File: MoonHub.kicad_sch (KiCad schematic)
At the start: 36 parts, among them U1 SRV05-4, U2 SRV05-4, U3 CH334U, U4 TPS2552DBVR, U5 SRV05-4, U6 SRV05-4, U7 SRV05-4, Y1 12MHz

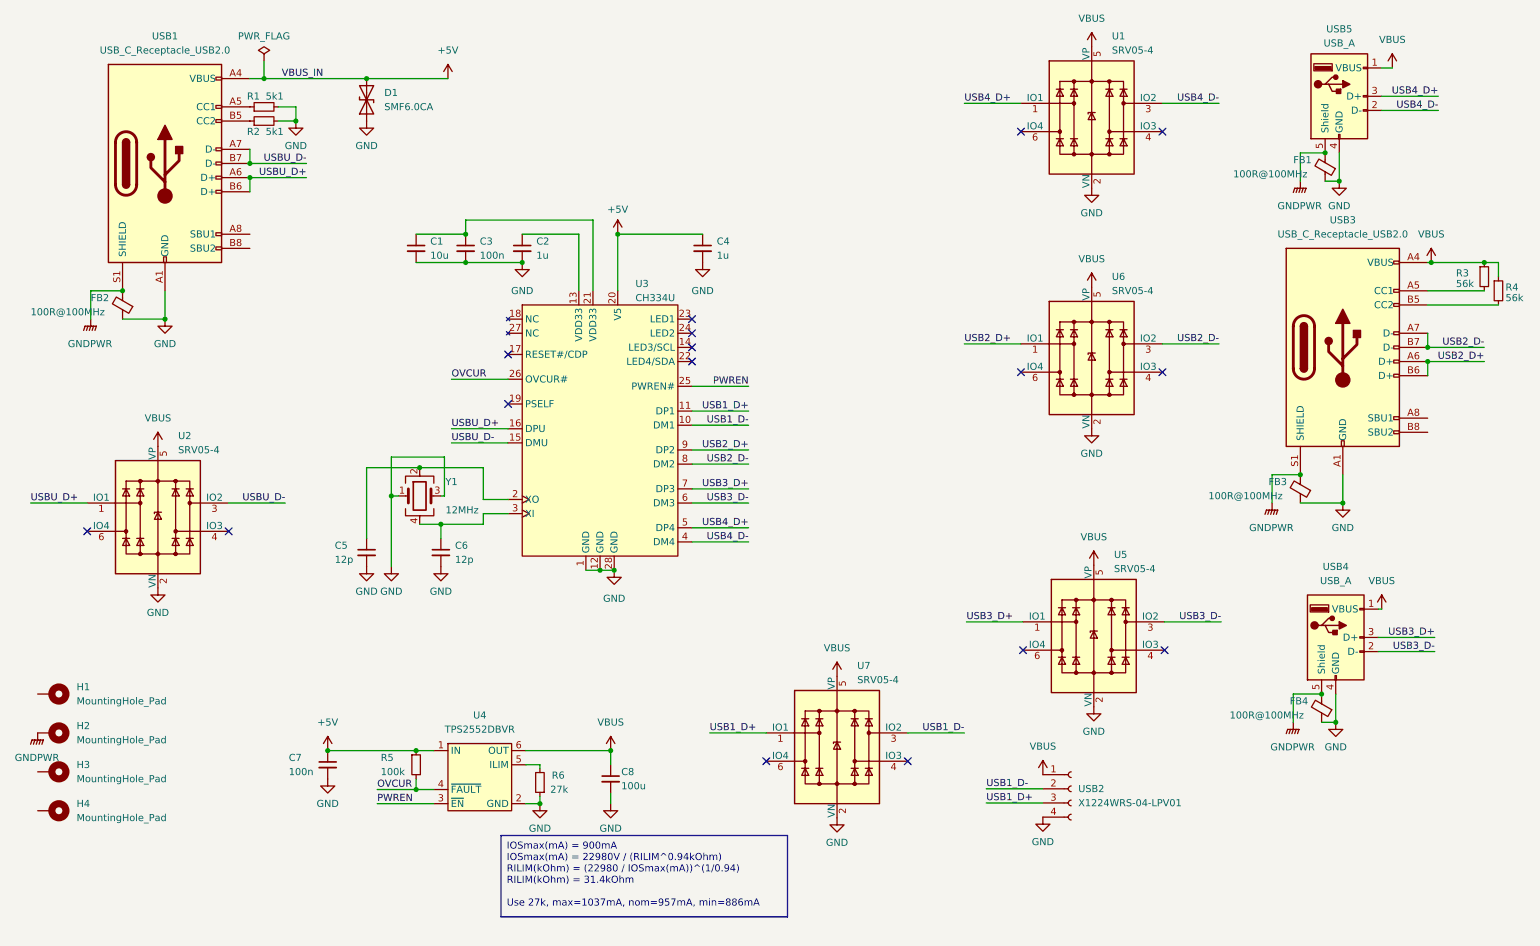
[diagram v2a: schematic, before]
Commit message: move uDB connector & switch current limit
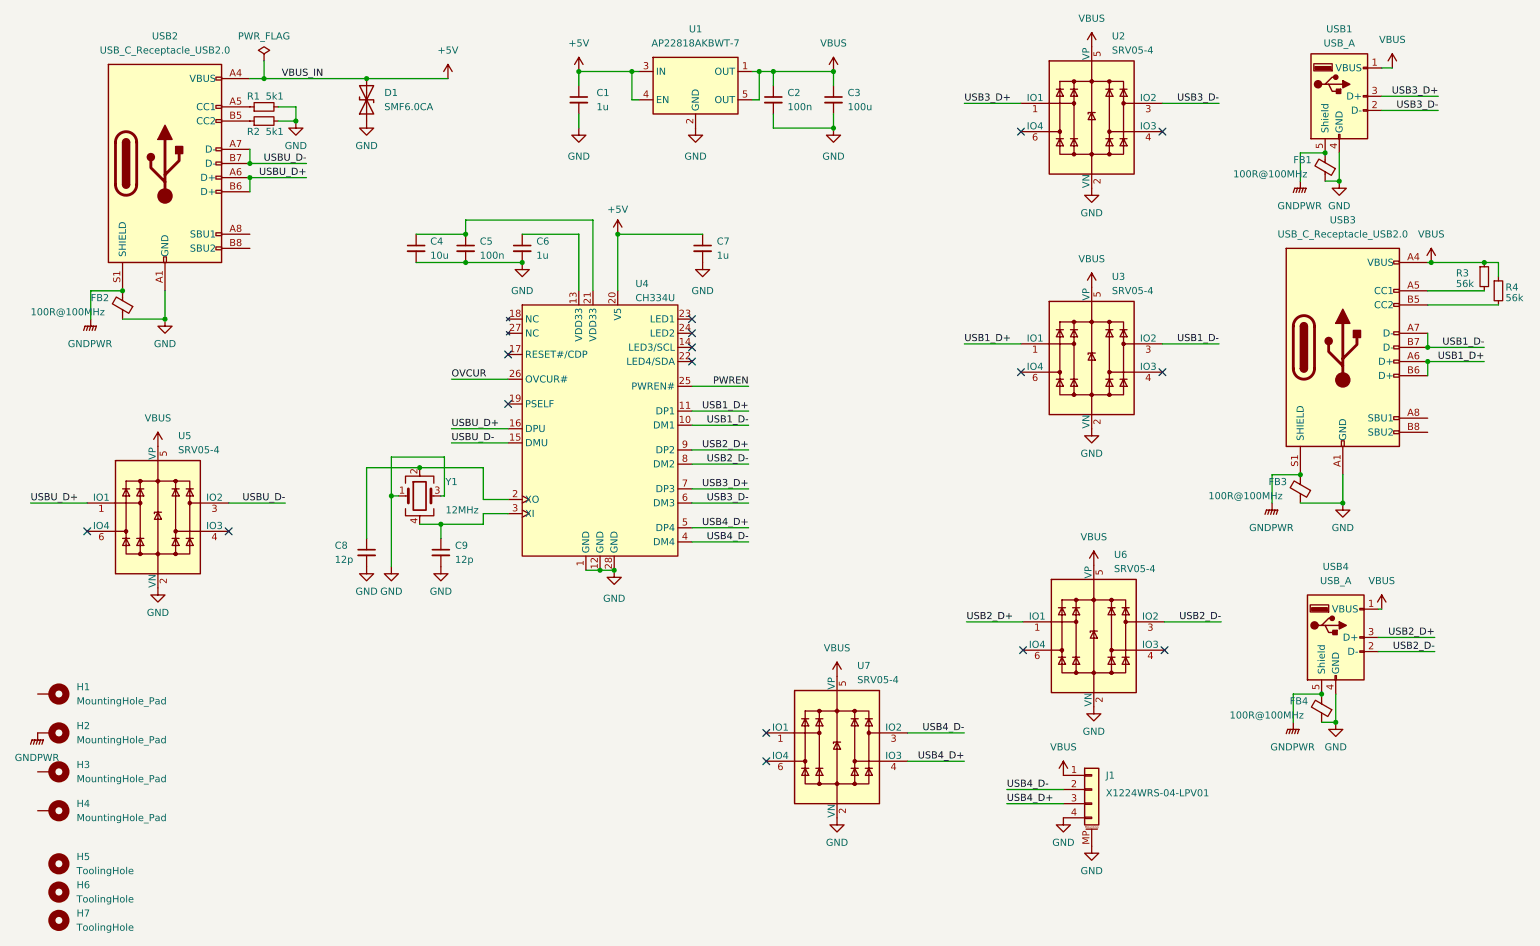
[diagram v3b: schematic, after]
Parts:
- removed C7: 100n, Capacitor_SMD:C_0805_2012Metric, symbol Device:C_Small
- removed C8: 100u, Capacitor_SMD:C_1206_3216Metric, symbol Device:C_Small
- removed R5: 100k, Resistor_SMD:R_0603_1608Metric, symbol Device:R_Small
- removed R6: 27k, Resistor_SMD:R_0603_1608Metric, symbol Device:R_Small
- removed U4: TPS2552DBVR, Package_TO_SOT_SMD:SOT-23-6, symbol MoonHub:TPS2552/53
- removed USB2: X1224WRS-04-LPV01, MoonHub:PicoEZMate-Reinforced-Lite, symbol Connector:Conn_01x04_Socket
- added C1: 1u, Capacitor_SMD:C_0402_1005Metric, symbol Device:C_Small
- added C2: 100n, Capacitor_SMD:C_0402_1005Metric, symbol Device:C_Small
- added C3: 100u, Capacitor_SMD:C_1206_3216Metric, symbol Device:C_Small
- added H5, H6, H7: ToolingHole, MoonHub:JLC-Tooling-Hole, symbol Mechanical:MountingHole
- added J1: X1224WRS-04-LPV01, MoonHub:UDB-PicoEZMate-Reinforced-Alt, symbol Connector_Generic_MountingPin:Conn_01x04_MountingPin
- added U1: AP22818AKBWT-7, Package_TO_SOT_SMD:SOT-23-5, symbol Power_Management:AP22814AW5
- C5: renamed from C3; footprint Capacitor_SMD:C_0805_2012Metric -> Capacitor_SMD:C_0402_1005Metric
- renumbered C1 to C4, C2 to C6, C4 to C7, C5 to C8, C6 to C9, U1 to U2, U6 to U3, U3 to U4, U2 to U5, U5 to U6, USB5 to USB1, USB1 to USB2
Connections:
- net +5V: now also C1.1, U1.3 (IN), U1.4 (EN)
- net GND: now also C1.2, C2.2, C3.2, J1.4 (Pin_4), J1.MP (MountPin), U1.2 (GND)
- net USB1_D+: now also U3.1 (IO1), USB3.A6 (D+), USB3.B6 (D+); no longer U7.1 (IO1)
- net USB1_D-: now also U3.3 (IO2), USB3.A7 (D-), USB3.B7 (D-); no longer U7.3 (IO2)
- net USB2_D+: now also U6.1 (IO1), USB4.3 (D+); no longer U3.1 (IO1), USB3.A6 (D+), USB3.B6 (D+)
- net USB2_D-: now also U6.3 (IO2), USB4.2 (D-); no longer U3.3 (IO2), USB3.A7 (D-), USB3.B7 (D-)
- net USB3_D+: now also U2.1 (IO1), USB1.3 (D+); no longer U6.1 (IO1), USB4.3 (D+)
- net USB3_D-: now also U2.3 (IO2), USB1.2 (D-); no longer U6.3 (IO2), USB4.2 (D-)
- net USB4_D+: now also U7.4 (IO3), J1.3 (Pin_3); no longer U2.1 (IO1), USB1.3 (D+)
- net USB4_D-: now also U7.3 (IO2), J1.2 (Pin_2); no longer U2.3 (IO2), USB1.2 (D-)
- net VBUS: now also C2.1, C3.1, J1.1 (Pin_1), U1.1 (OUT), U1.5 (OUT)

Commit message: redo esd protection
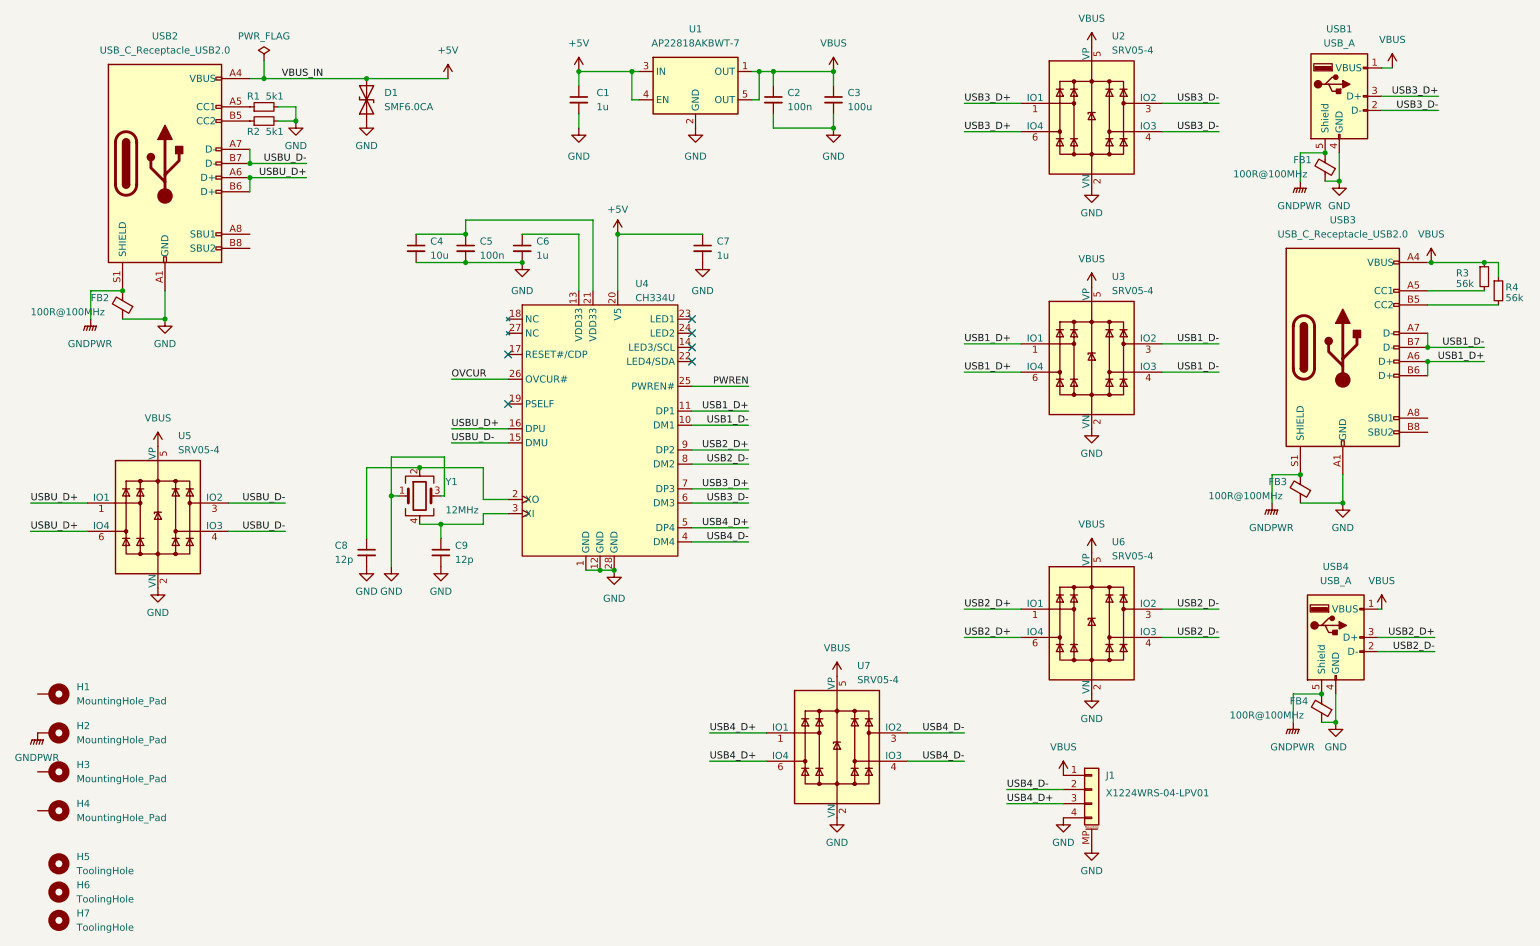
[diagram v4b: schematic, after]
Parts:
- U2, U3, U5, U6, U7: footprint PCM_marbastlib-various:SOT-23-6-routable -> Package_TO_SOT_SMD:SOT-23-6
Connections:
- net USB1_D+: now also U3.6 (IO4)
- net USB1_D-: now also U3.4 (IO3)
- net USB2_D+: now also U6.6 (IO4)
- net USB2_D-: now also U6.4 (IO3)
- net USB3_D+: now also U2.6 (IO4)
- net USB3_D-: now also U2.4 (IO3)
- net USB4_D+: now also U7.1 (IO1), U7.6 (IO4); no longer U7.4 (IO3)
- net USB4_D-: now also U7.4 (IO3)
- net USBU_D+: now also U5.6 (IO4)
- net USBU_D-: now also U5.4 (IO3)
- no-connect marks 16 -> 6
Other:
- moved on the sheet: U6

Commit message: change usb esd array
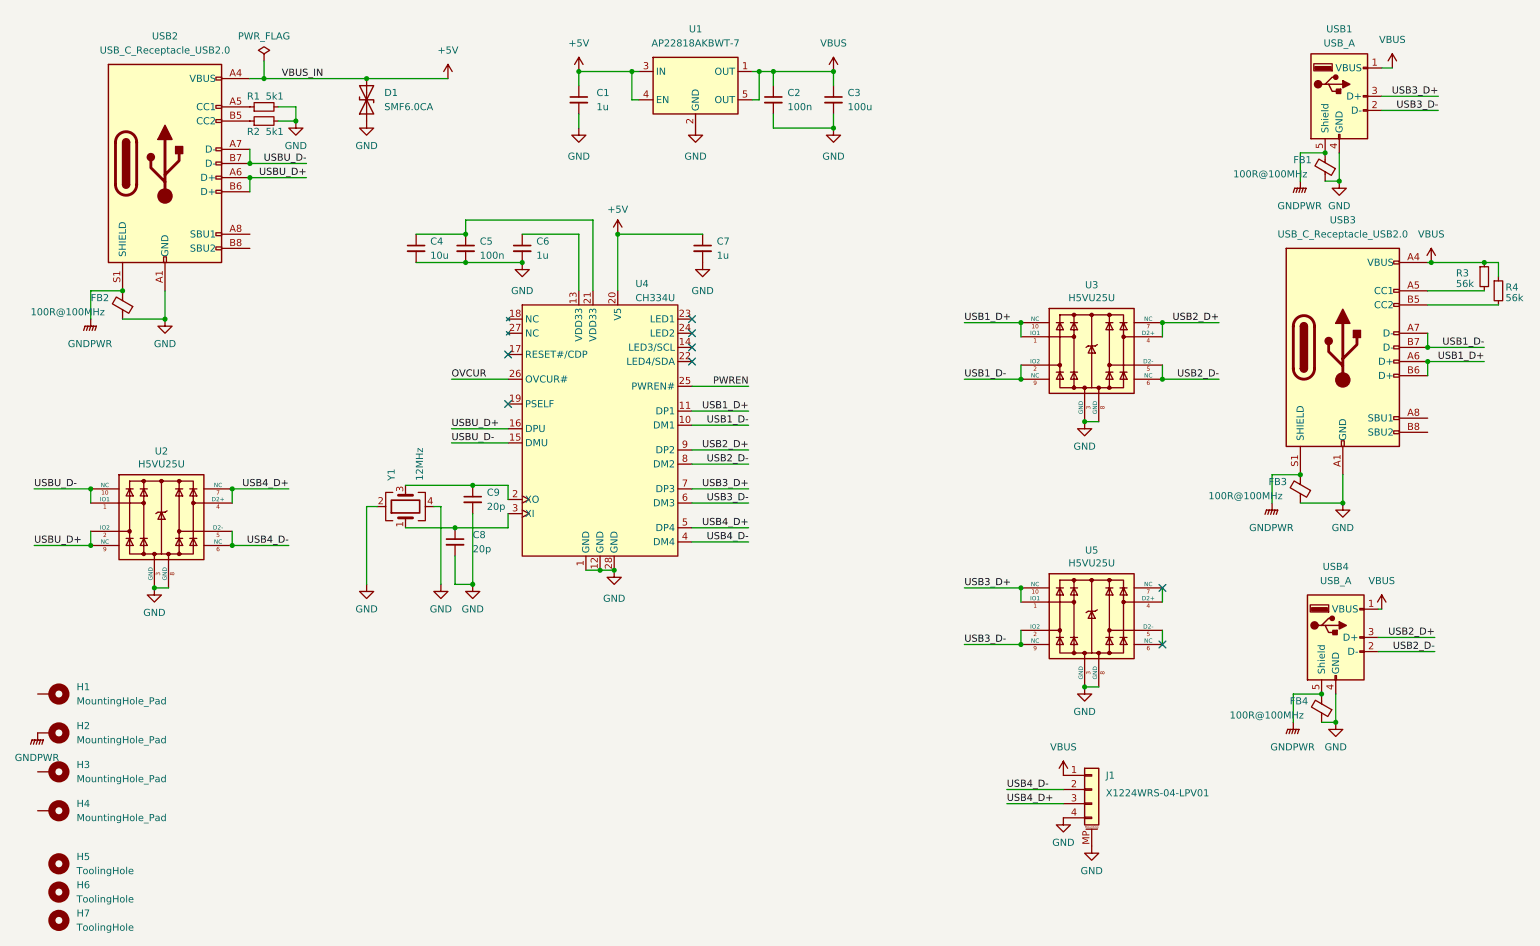
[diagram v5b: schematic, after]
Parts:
- removed U2, U3, U5, U6, U7: SRV05-4, Package_TO_SOT_SMD:SOT-23-6, symbol PCM_marbastlib-various:SRV05-4
- added U2, U3, U5: H5VU25U, MoonHub:DFN2510, symbol Unified-Daughterboard-rescue:TPD4E05U06DQAR-acheronSymbols
- C8, C9: value 12p -> 20p
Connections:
- net GND: now also Y1.2, Y1.4, U2.3 (GND), U2.8 (GND), U3.3 (GND), U3.8 (GND), U5.3 (GND), U5.8 (GND); no longer Y1.1, Y1.3
- net USB1_D+: now also U3.1 (IO1), U3.10 (NC)
- net USB1_D-: now also U3.2 (IO2), U3.9 (NC)
- net USB2_D+: now also U3.4 (D2+), U3.7 (NC)
- net USB2_D-: now also U3.5 (D2-), U3.6 (NC)
- net USB3_D+: now also U5.1 (IO1), U5.10 (NC)
- net USB3_D-: now also U5.2 (IO2), U5.9 (NC)
- net USB4_D+: now also U2.4 (D2+), U2.7 (NC)
- net USB4_D-: now also U2.5 (D2-), U2.6 (NC)
- net USBU_D+: now also U2.2 (IO2), U2.9 (NC)
- net USBU_D-: now also U2.1 (IO1), U2.10 (NC)
- new net: C8.1, U4.3 (XI), Y1.1
- new net: C9.1, U4.2 (XO), Y1.3
- new net: U5.4 (D2+), U5.7 (NC)
- new net: U5.5 (D2-), U5.6 (NC)
- no-connect marks 6 -> 8
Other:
- moved on the sheet: Y1

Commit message: remove ferrites
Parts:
- removed D1: SMF6.0CA, MoonHub:SOD-123FL_L2.8-W1.8-LS3.7-BI, symbol Device:D_TVS
- removed FB1, FB2, FB3, FB4: 100R@100MHz, Inductor_SMD:L_0805_2012Metric, symbol Device:FerriteBead_Small
- removed H1, H3, H4: MountingHole_Pad, MoonHub:Generic-Mounthole, symbol Mechanical:MountingHole_Pad
- added D1: SMAJ5.0A, Diode_SMD:D_SMA, symbol Diode:SMAJ5.0A
- added H1, H3, H4: MountingHole, MountingHole:MountingHole_2.2mm_M2_ISO7380, symbol Mechanical:MountingHole
- C1: value 1u -> 10u; footprint Capacitor_SMD:C_0402_1005Metric -> Capacitor_SMD:C_0805_2012Metric
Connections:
- net +5V: now also D1.1 (A1)
- net GND: now also D1.2 (A2); no longer J1.MP (MountPin)
- net GNDPWR: now also J1.MP (MountPin)
- no-connect marks 8 -> 10
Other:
- moved on the sheet: J1
